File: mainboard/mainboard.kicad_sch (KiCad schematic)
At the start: 31 parts, among them J1 Barrel_Jack 2.1mm / 2.5A, J2 Screw_Terminal_01x05, J3 Screw_Terminal_01x04, J4 Conn_02x04_Odd_Even, Q1 IRF3708, Q2 IRF3708, Q3 IRF3708, U1 VR10S05, U2 ATmega328P-P, Y1 16Mhz, 20pF

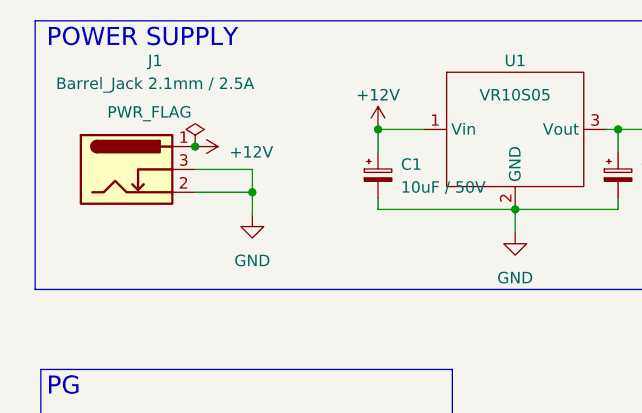
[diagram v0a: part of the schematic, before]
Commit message: added fuse, modified trace widths and added fabrication files
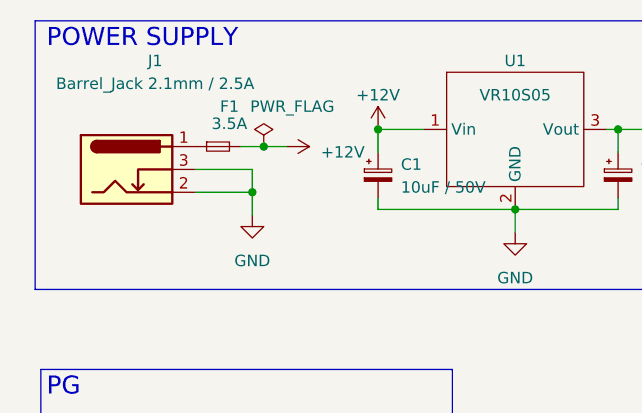
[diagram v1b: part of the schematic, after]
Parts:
- added F1: 3.5A, Resistor_SMD:R_1206_3216Metric, symbol Device:Fuse_Small
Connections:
- net +12V: now also F1.2; no longer J1.1
- new net: F1.1, J1.1

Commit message: minor changes
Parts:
- R1: value 500 -> 500 / 1/4W
- R2: value 150 -> 150 / 1/10W
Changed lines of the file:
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@@
   (junction (at 260.35 71.12) (diameter 0) (color 0 0 0 0)
   )
+  (junction (at 32.385 33.02) (diameter 0) (color 0 0 0 0)
+  )
   (junction (at 77.47 26.035) (diameter 0) (color 0 0 0 0)
   )
@@
   )
   (junction (at 232.41 39.37) (diameter 0) (color 0 0 0 0)
-  )
-  (junction (at 232.41 125.73) (diameter 0) (color 0 0 0 0)
   )
   (junction (at 260.35 78.74) (diameter 0) (color 0 0 0 0)
@@
     (stroke (width 0) (type default))
   )
+  (wire (pts (xy 32.385 33.02) (xy 36.83 33.02))
+    (stroke (width 0) (type default))
+  )
   (wire (pts (xy 35.56 27.94) (xy 38.1 27.94))
     (stroke (width 0) (type default))
   )
-  (wire (pts (xy 30.48 33.02) (xy 36.83 33.02))
+  (wire (pts (xy 30.48 33.02) (xy 32.385 33.02))
     (stroke (width 0) (type default))
   )
@@
     )
   )
+  (symbol (lib_id "power:PWR_FLAG") (at 32.385 33.02 180) (unit 1)
+    (in_bom yes) (on_board yes) (dnp no)
+    (property "Reference" "#FLG03" (at 32.385 34.925 0)
+      (effects (font (size 1.27 1.27)) hide)
+    )
+    (property "Value" "PWR_FLAG" (at 29.21 37.465 0)
+      (effects (font (size 1.27 1.27)))
+    )
+    (property "Footprint" "" (at 32.385 33.02 0)
+      (effects (font (size 1.27 1.27)) hide)
+    )
+    (property "Datasheet" "~" (at 32.385 33.02 0)
+      (effects (font (size 1.27 1.27)) hide)
+    )
+    (pin "1")
+    (instances
+      (project "mainboard"
+        (path "/377ddc21-dd4e-4c61-979e-9bf1c54796f9"
+          (reference "#FLG03") (unit 1)
+        )
+      )
+    )
+  )
   (symbol (lib_id "Connector_Generic:Conn_02x04_Odd_Even") (at 241.935 151.13 0) (unit 1)
     (in_bom yes) (on_board yes) (dnp no) (fields_autoplaced)
@@
       (effects (font (size 1.27 1.27)))
     )
-    (property "Value" "500" (at 29.845 64.77 90)
+    (property "Value" "500 / 1/4W" (at 29.845 67.945 90)
       (effects (font (size 1.27 1.27)))
     )
@@
     )
   )
-  (symbol (lib_id "power:PWR_FLAG") (at 232.41 125.73 270) (unit 1)
-    (in_bom yes) (on_board yes) (dnp no) (fields_autoplaced)
-    (property "Reference" "#FLG02" (at 234.315 125.73 0)
-      (effects (font (size 1.27 1.27)) hide)
-    )
-    (property "Value" "PWR_FLAG" (at 235.585 126.365 90)
-      (effects (font (size 1.27 1.27)) (justify left))
-    )
-    (property "Footprint" "" (at 232.41 125.73 0)
-      (effects (font (size 1.27 1.27)) hide)
-    )
-    (property "Datasheet" "~" (at 232.41 125.73 0)
-      (effects (font (size 1.27 1.27)) hide)
-    )
-    (pin "1")
-    (instances
-      (project "mainboard"
-        (path "/377ddc21-dd4e-4c61-979e-9bf1c54796f9"
-          (reference "#FLG02") (unit 1)
-        )
-      )
-    )
-  )
   (symbol (lib_id "Device:LED_Small") (at 45.72 64.77 180) (unit 1)
     (in_bom yes) (on_board yes) (dnp no) (fields_autoplaced)
@@
       (effects (font (size 1.27 1.27)))
     )
-    (property "Value" "150" (at 50.8 64.77 90)
-      (effects (font (size 1.27 1.27)))
-    )
+    (property "Value" "150 / 1/10W" (at 50.8 67.945 90)
+      (effects (font (size 1.27 1.27)))
+    )
